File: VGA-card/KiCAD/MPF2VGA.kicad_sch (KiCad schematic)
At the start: 27 parts, among them U1 74LVC245, U2 74LVC245, U3 74LVC245, U4 74LS07, U5 UA78M33CKCS, U6 Pico

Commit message: KiCAD project renamed
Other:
- title: Apple II VGA Card -> MPF-II VGA Card
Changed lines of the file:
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@@
   (paper "A4")
   (title_block
-    (title "Apple II VGA Card")
-    (date "2022-09-08")
+    (title "MPF-II VGA Card")
+    (date "2022-09-14")
     (rev "A")
     (comment 1 "Licensed under CERN-OHL-P V2.0 (https://ohwr.org/cern_ohl_p_v2.txt)")
     (comment 2 "Copyright (c) 2021-2022 Mark Aikens")
+    (comment 3 "Modified fpr MPF2 by Random DIY")
   )
   (junction (at 38.1 189.23) (diameter 0) (color 0 0 0 0)

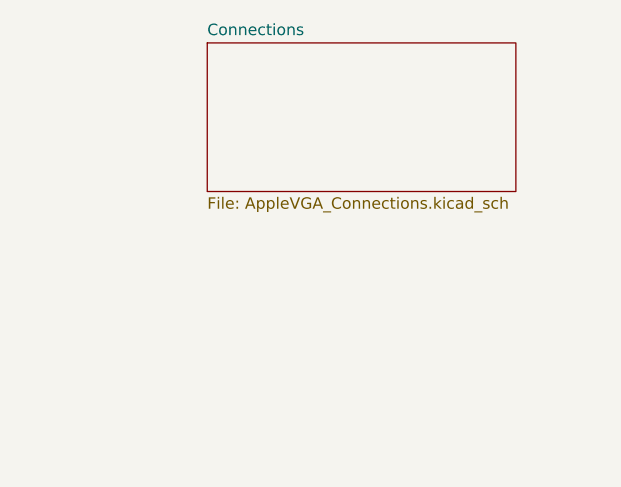
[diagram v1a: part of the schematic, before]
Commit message: KiCAD connections sheet renamed
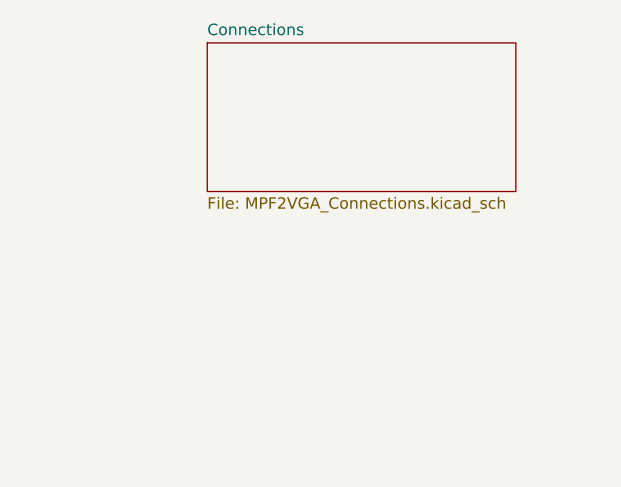
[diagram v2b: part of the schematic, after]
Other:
- sheet Connections: file AppleVGA_Connections.kicad_sch -> MPF2VGA_Connections.kicad_sch
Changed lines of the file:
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@@
       (effects (font (size 1.27 1.27)) (justify left bottom))
     )
-    (property "Sheet file" "AppleVGA_Connections.kicad_sch" (id 1) (at 306.07 29.7946 0)
+    (property "Sheet file" "MPF2VGA_Connections.kicad_sch" (id 1) (at 306.07 29.7946 0)
       (effects (font (size 1.27 1.27)) (justify left top))
     )
@@
       (reference "#PWR0112") (unit 1) (value "+3.3V") (footprint "")
     )
-    (path "/00000000-0000-0000-0000-0000619081b0/00000000-0000-0000-0000-000061948241"
-      (reference "#PWR0113") (unit 1) (value "GND") (footprint "")
-    )
-    (path "/00000000-0000-0000-0000-0000619081b0/00000000-0000-0000-0000-00006194824c"
-      (reference "#PWR0114") (unit 1) (value "GND") (footprint "")
-    )
-    (path "/00000000-0000-0000-0000-0000619081b0/00000000-0000-0000-0000-0000618fb32a"
-      (reference "#PWR0115") (unit 1) (value "+3.3V") (footprint "")
-    )
-    (path "/00000000-0000-0000-0000-0000619081b0/00000000-0000-0000-0000-0000618fb330"
-      (reference "#PWR0116") (unit 1) (value "GND") (footprint "")
-    )
     (path "/00000000-0000-0000-0000-0000619d3827"
       (reference "#PWR0117") (unit 1) (value "+3.3V") (footprint "")
-    )
-    (path "/00000000-0000-0000-0000-0000619081b0/00000000-0000-0000-0000-000061914acb"
-      (reference "#PWR0118") (unit 1) (value "GND") (footprint "")
     )
     (path "/00000000-0000-0000-0000-000061a22b6c"
       (reference "#PWR0119") (unit 1) (value "GND") (footprint "")
     )
+    (path "/00000000-0000-0000-0000-0000619081b0/00000000-0000-0000-0000-0000618fb32a"
+      (reference "#PWR?") (unit 1) (value "+3.3V") (footprint "")
+    )
+    (path "/00000000-0000-0000-0000-0000619081b0/00000000-0000-0000-0000-0000618fb330"
+      (reference "#PWR?") (unit 1) (value "GND") (footprint "")
+    )
+    (path "/00000000-0000-0000-0000-0000619081b0/00000000-0000-0000-0000-000061914acb"
+      (reference "#PWR?") (unit 1) (value "GND") (footprint "")
+    )
+    (path "/00000000-0000-0000-0000-0000619081b0/00000000-0000-0000-0000-000061948241"
+      (reference "#PWR?") (unit 1) (value "GND") (footprint "")
+    )
+    (path "/00000000-0000-0000-0000-0000619081b0/00000000-0000-0000-0000-00006194824c"
+      (reference "#PWR?") (unit 1) (value "GND") (footprint "")
+    )
     (path "/00000000-0000-0000-0000-0000619081b0/00000000-0000-0000-0000-000061b1399a"
-      (reference "#PWR0120") (unit 1) (value "GND") (footprint "")
+      (reference "#PWR?") (unit 1) (value "GND") (footprint "")
     )
     (path "/00000000-0000-0000-0000-0000619081b0/00000000-0000-0000-0000-000061b139a4"
-      (reference "#PWR0121") (unit 1) (value "+5V") (footprint "")
+      (reference "#PWR?") (unit 1) (value "+5V") (footprint "")
     )
     (path "/00000000-0000-0000-0000-0000619081b0/00000000-0000-0000-0000-0000618fb312"
